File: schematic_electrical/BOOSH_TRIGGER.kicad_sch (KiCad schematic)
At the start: 15 parts, among them Q1 FQP27P06, Q2 FQP27P06, U4 ULN2803A

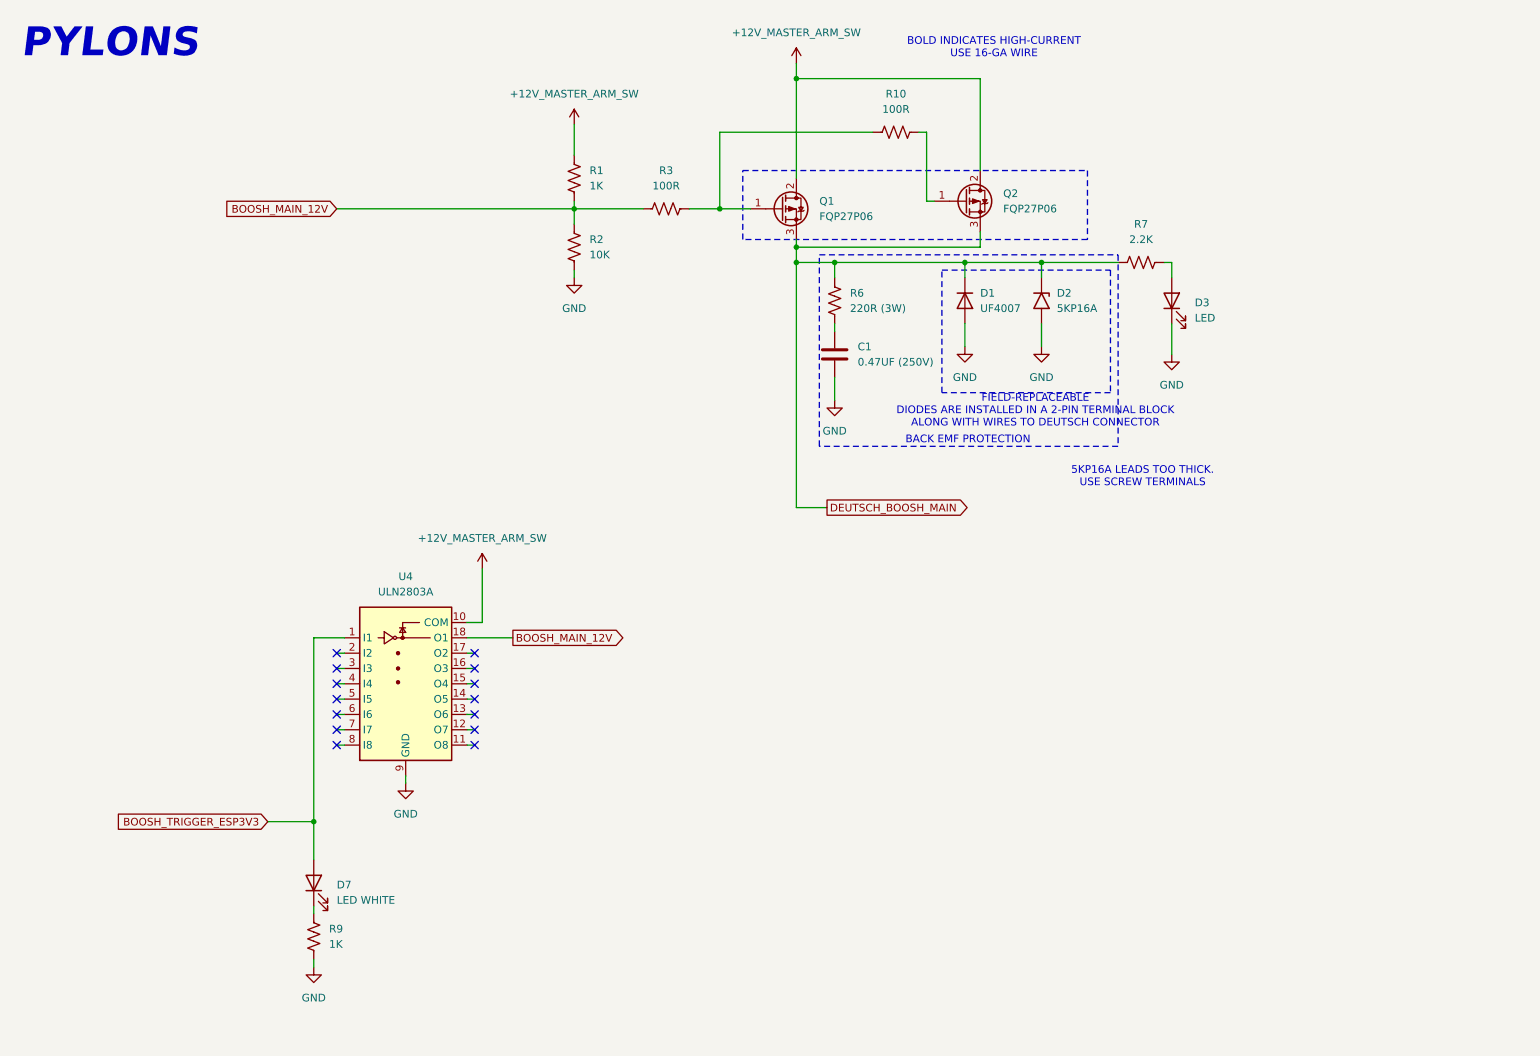
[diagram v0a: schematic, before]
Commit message: Schematic for bar: use ULN2308 for button 12V lamps
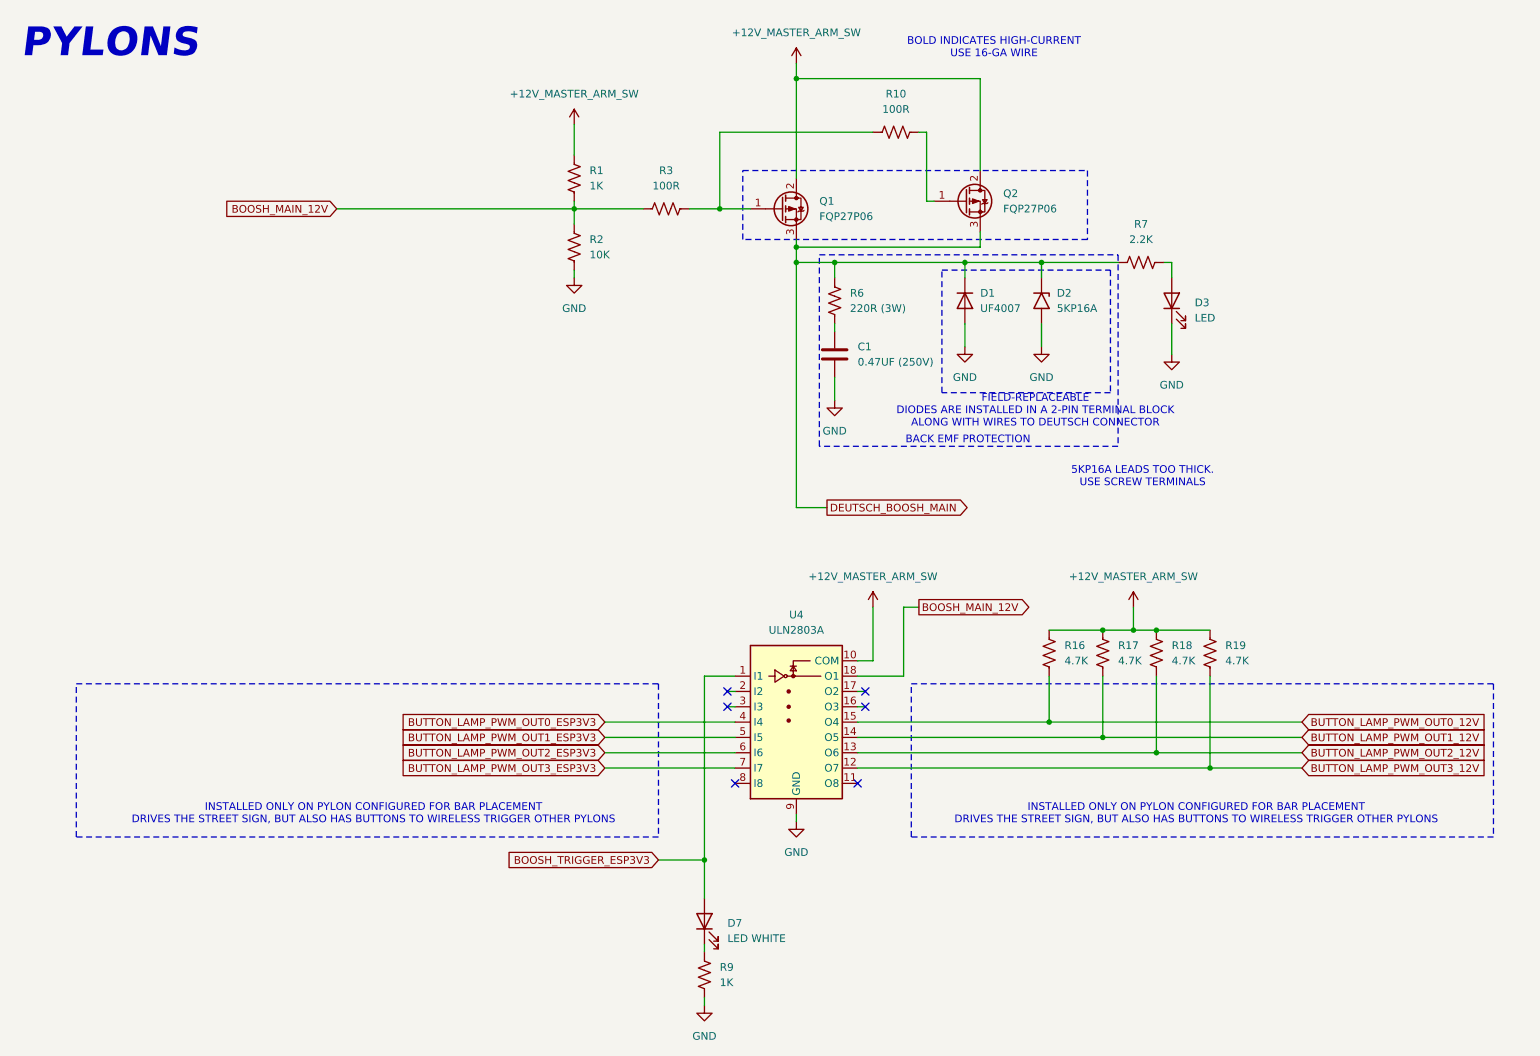
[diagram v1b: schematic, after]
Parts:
- added R16, R17, R18, R19: 4.7K, symbol Device:R_US
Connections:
- net +12V_MASTER_ARM_SW: now also R16.1, R17.1, R18.1, R19.1
- net BUTTON_LAMP_PWM_OUT3_12V: now reaches U4.12 (O7)
- net BUTTON_LAMP_PWM_OUT3_12V: now also R19.2
- net BUTTON_LAMP_PWM_OUT2_12V: now reaches U4.13 (O6)
- net BUTTON_LAMP_PWM_OUT2_12V: now also R18.2
- net BUTTON_LAMP_PWM_OUT1_12V: now reaches U4.14 (O5)
- net BUTTON_LAMP_PWM_OUT1_12V: now also R17.2
- net BUTTON_LAMP_PWM_OUT0_12V: now reaches U4.15 (O4)
- net BUTTON_LAMP_PWM_OUT0_12V: now also R16.2
- net BUTTON_LAMP_PWM_OUT0_ESP3V3: now reaches U4.4 (I4)
- net BUTTON_LAMP_PWM_OUT1_ESP3V3: now reaches U4.5 (I5)
- net BUTTON_LAMP_PWM_OUT2_ESP3V3: now reaches U4.6 (I6)
- net BUTTON_LAMP_PWM_OUT3_ESP3V3: now reaches U4.7 (I7)
- no-connect marks 14 -> 6
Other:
- note added: "INSTALLED ONLY ON PYLON CONFIGURED FOR BAR PLACEMENT DRIVES THE STREET SIGN, BUT ALSO HAS BUTTONS TO WIRELESS TRIGGER OTHER PYLONS"
- moved on the sheet: D7, R9, U4

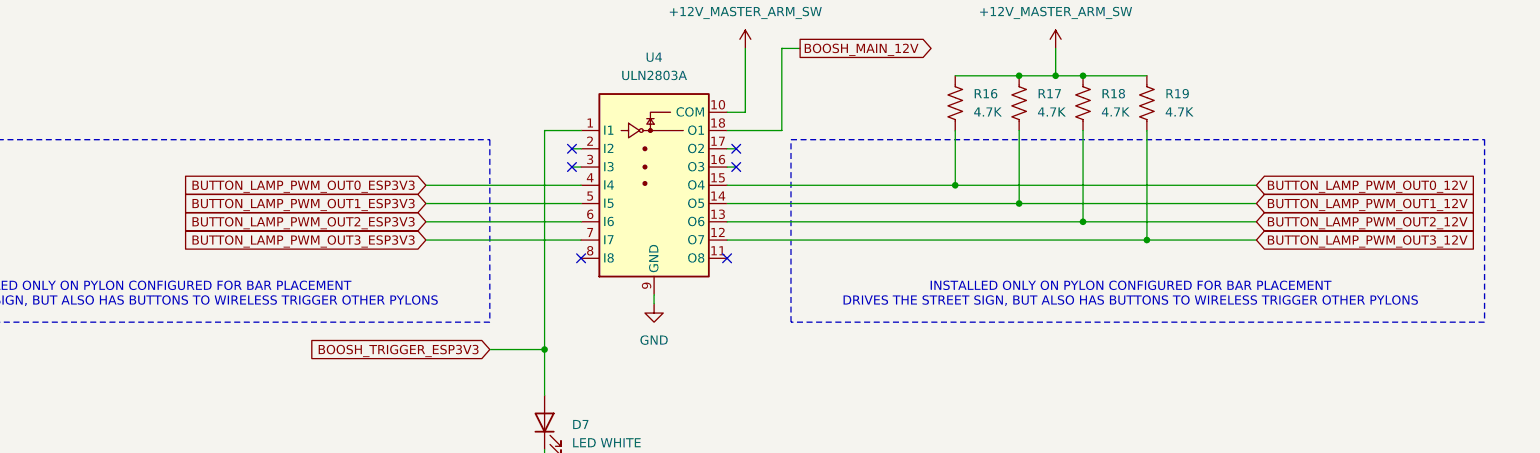
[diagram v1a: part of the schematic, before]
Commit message: Schematic as built for bar box. 12V fire enable switch wired in correct manner such that LED is off when switch is off.
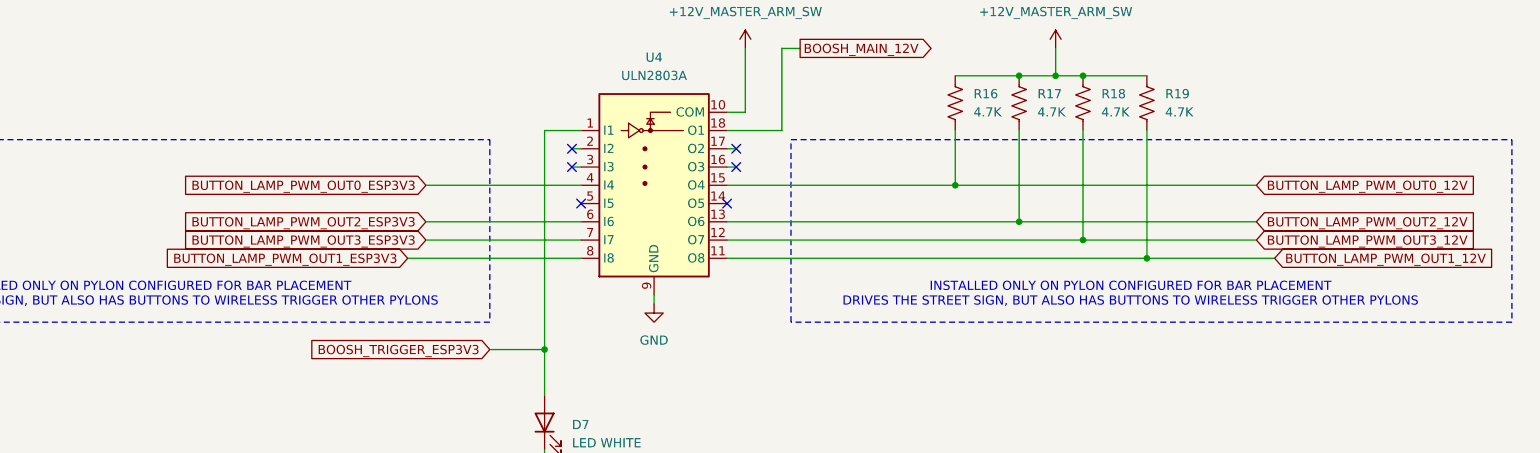
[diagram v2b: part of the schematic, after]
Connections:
- net BUTTON_LAMP_PWM_OUT1_12V: now also R19.2, U4.11 (O8); no longer R17.2, U4.14 (O5)
- net BUTTON_LAMP_PWM_OUT1_ESP3V3: now also U4.8 (I8); no longer U4.5 (I5)
- net BUTTON_LAMP_PWM_OUT2_12V: now also R17.2; no longer R18.2
- net BUTTON_LAMP_PWM_OUT3_12V: now also R18.2; no longer R19.2
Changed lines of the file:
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@@
-	)
-	(junction
-		(at 212.09 140.97)
-		(diameter 0)
-		(color 0 0 0 0)
 	)
 	(junction
@@
 	)
 	(junction
+		(at 212.09 143.51)
+		(diameter 0)
+		(color 0 0 0 0)
+	)
+	(junction
+		(at 185.42 133.35)
+		(diameter 0)
+		(color 0 0 0 0)
+	)
+	(junction
 		(at 203.2 118.11)
 		(diameter 0)
@@
 	)
 	(junction
-		(at 185.42 133.35)
-		(diameter 0)
-		(color 0 0 0 0)
-	)
-	(junction
-		(at 203.2 138.43)
+		(at 194.31 138.43)
+		(diameter 0)
+		(color 0 0 0 0)
+	)
+	(junction
+		(at 203.2 140.97)
 		(diameter 0)
 		(color 0 0 0 0)
@@
 	(junction
 		(at 149.86 57.15)
-		(diameter 0)
-		(color 0 0 0 0)
-	)
-	(junction
-		(at 194.31 135.89)
 		(diameter 0)
 		(color 0 0 0 0)
@@
 	)
 	(no_connect
+		(at 133.35 135.89)
+	)
+	(no_connect
 		(at 154.94 130.81)
 	)
 	(no_connect
-		(at 133.35 143.51)
-	)
-	(no_connect
-		(at 153.67 143.51)
+		(at 153.67 135.89)
 	)
 	(wire
@@
 	(wire
 		(pts
-			(xy 227.33 140.97) (xy 212.09 140.97)
+			(xy 153.67 140.97) (xy 203.2 140.97)
 		)
 		(stroke
@@
 	(wire
 		(pts
-			(xy 194.31 125.73) (xy 194.31 135.89)
-		)
-		(stroke
-			(width 0)
-			(type default)
-		)
-	)
-	(wire
-		(pts
-			(xy 203.2 138.43) (xy 153.67 138.43)
-		)
-		(stroke
-			(width 0)
-			(type default)
-		)
-	)
-	(wire
-		(pts
 			(xy 173.99 54.61) (xy 143.51 54.61)
 		)
@@
 	(wire
 		(pts
-			(xy 111.76 135.89) (xy 133.35 135.89)
-		)
-		(stroke
-			(width 0)
-			(type default)
-		)
-	)
-	(wire
-		(pts
 			(xy 199.39 114.3) (xy 199.39 118.11)
 		)
@@
 	(wire
 		(pts
+			(xy 212.09 125.73) (xy 212.09 143.51)
+		)
+		(stroke
+			(width 0)
+			(type default)
+		)
+	)
+	(wire
+		(pts
+			(xy 109.22 143.51) (xy 133.35 143.51)
+		)
+		(stroke
+			(width 0)
+			(type default)
+		)
+	)
+	(wire
+		(pts
 			(xy 163.83 114.3) (xy 161.29 114.3)
 		)
@@
 	(wire
 		(pts
+			(xy 203.2 125.73) (xy 203.2 140.97)
+		)
+		(stroke
+			(width 0)
+			(type default)
+		)
+	)
+	(wire
+		(pts
 			(xy 156.21 114.3) (xy 156.21 123.19)
 		)
@@
 	(wire
 		(pts
-			(xy 194.31 135.89) (xy 153.67 135.89)
+			(xy 153.67 143.51) (xy 212.09 143.51)
 		)
 		(stroke
@@
 	(wire
 		(pts
+			(xy 185.42 133.35) (xy 227.33 133.35)
+		)
+		(stroke
+			(width 0)
+			(type default)
+		)
+	)
+	(wire
+		(pts
 			(xy 161.29 125.73) (xy 153.67 125.73)
 		)
@@
 	(wire
 		(pts
-			(xy 212.09 140.97) (xy 153.67 140.97)
-		)
-		(stroke
-			(width 0)
-			(type default)
-		)
-	)
-	(wire
-		(pts
 			(xy 67.31 48.26) (xy 106.68 48.26)
 		)
@@
 	(wire
 		(pts
-			(xy 203.2 125.73) (xy 203.2 138.43)
+			(xy 212.09 143.51) (xy 229.87 143.51)
 		)
 		(stroke
@@
 	(wire
 		(pts
-			(xy 227.33 135.89) (xy 194.31 135.89)
+			(xy 194.31 138.43) (xy 227.33 138.43)
 		)
 		(stroke
@@
 	(wire
 		(pts
+			(xy 194.31 125.73) (xy 194.31 138.43)
+		)
+		(stroke
+			(width 0)
+			(type default)
+		)
+	)
+	(wire
+		(pts
 			(xy 143.51 53.34) (xy 143.51 54.61)
 		)
@@
 	(wire
 		(pts
-			(xy 227.33 133.35) (xy 185.42 133.35)
+			(xy 153.67 133.35) (xy 185.42 133.35)
 		)
 		(stroke
@@
 	(wire
 		(pts
-			(xy 212.09 125.73) (xy 212.09 140.97)
-		)
-		(stroke
-			(width 0)
-			(type default)
-		)
-	)
-	(wire
-		(pts
 			(xy 143.51 97.79) (xy 148.59 97.79)
 		)
@@
 	(wire
 		(pts
-			(xy 227.33 138.43) (xy 203.2 138.43)
-		)
-		(stroke
-			(width 0)
-			(type default)
-		)
-	)
-	(wire
-		(pts
-			(xy 185.42 133.35) (xy 153.67 133.35)
+			(xy 153.67 138.43) (xy 194.31 138.43)
+		)
+		(stroke
+			(width 0)
+			(type default)
+		)
+	)
+	(wire
+		(pts
+			(xy 203.2 140.97) (xy 227.33 140.97)
 		)
 		(stroke
@@
 	(rectangle
 		(start 162.56 127)
-		(end 259.08 152.4)
+		(end 262.89 152.4)
 		(stroke
 			(width 0)
@@
 	(global_label "BUTTON_LAMP_PWM_OUT1_ESP3V3"
 		(shape input)
-		(at 111.76 135.89 180)
+		(at 109.22 143.51 180)
 		(fields_autoplaced yes)
 		(effects
@@
 		)
 		(property "Intersheetrefs" "${INTERSHEET_REFS}"
-			(at 76.7226 135.89 0)
+			(at 74.1826 143.51 0)
 			(effects
 				(font
@@
 	(global_label "BUTTON_LAMP_PWM_OUT1_12V"
 		(shape input)
-		(at 227.33 135.89 0)
+		(at 229.87 143.51 0)
 		(fields_autoplaced yes)
 		(effects
@@
 		)
 		(property "Intersheetrefs" "${INTERSHEET_REFS}"
-			(at 258.7389 135.89 0)
+			(at 261.2789 143.51 0)
 			(effects
 				(font
